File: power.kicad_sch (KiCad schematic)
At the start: 37 parts, among them J6 Conn_01x02, Q1 AO3401A, SW1 MSK12C02, U1 TP4056-42-ESOP8, U2 EA3036C

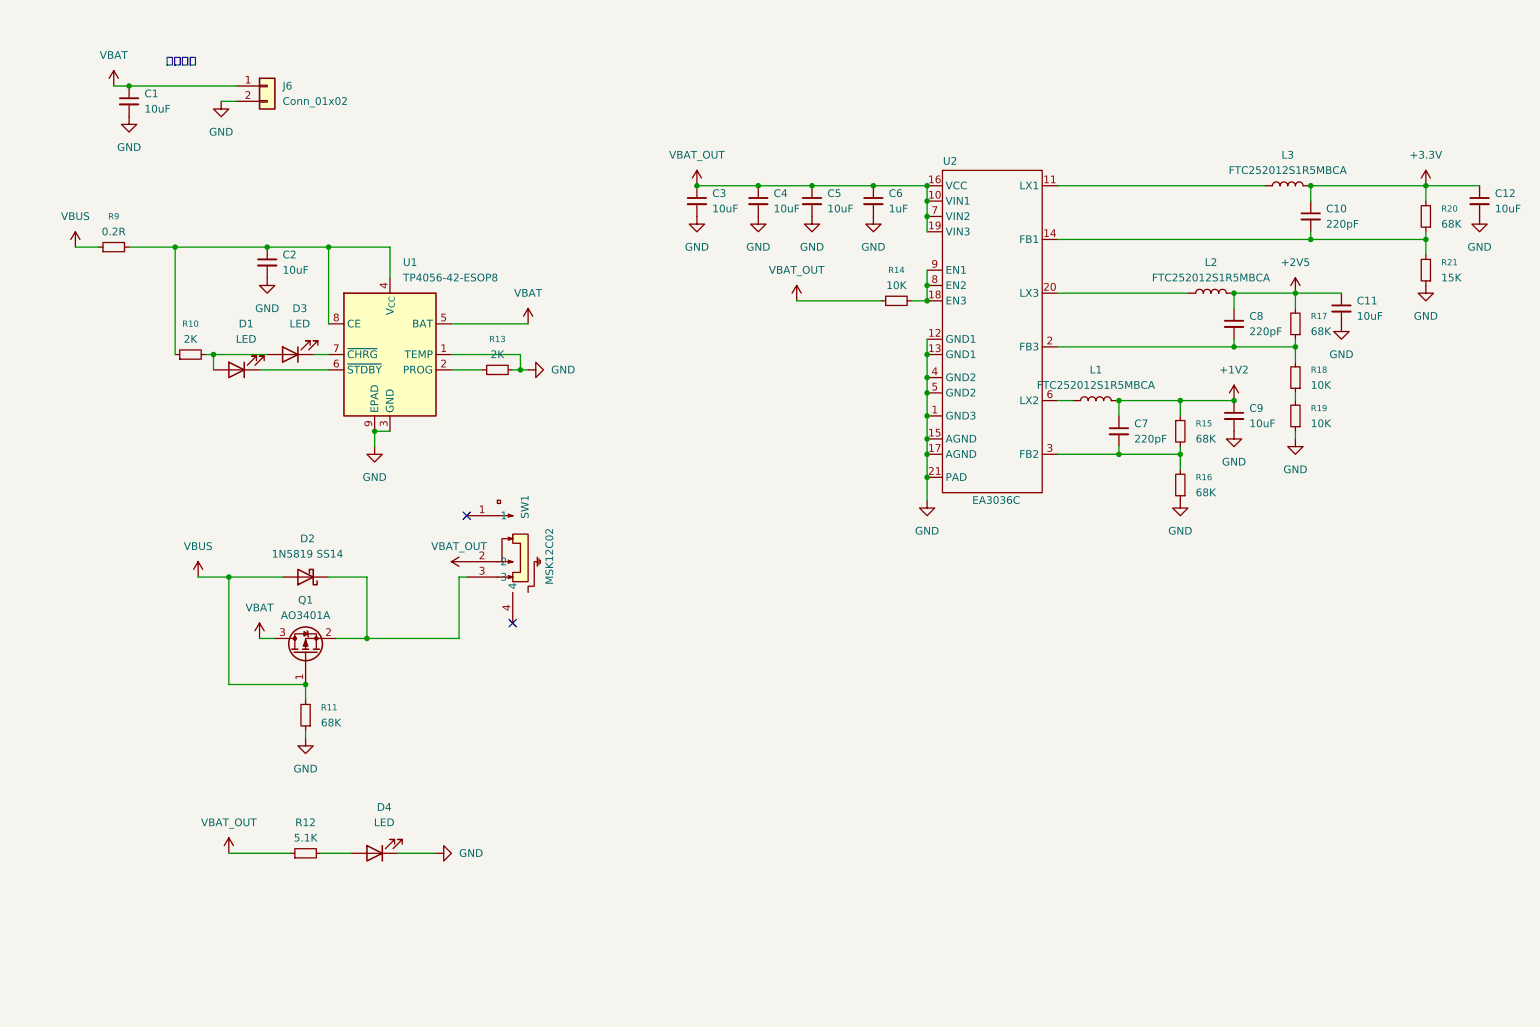
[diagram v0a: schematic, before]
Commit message: V0.3.1 bugfix
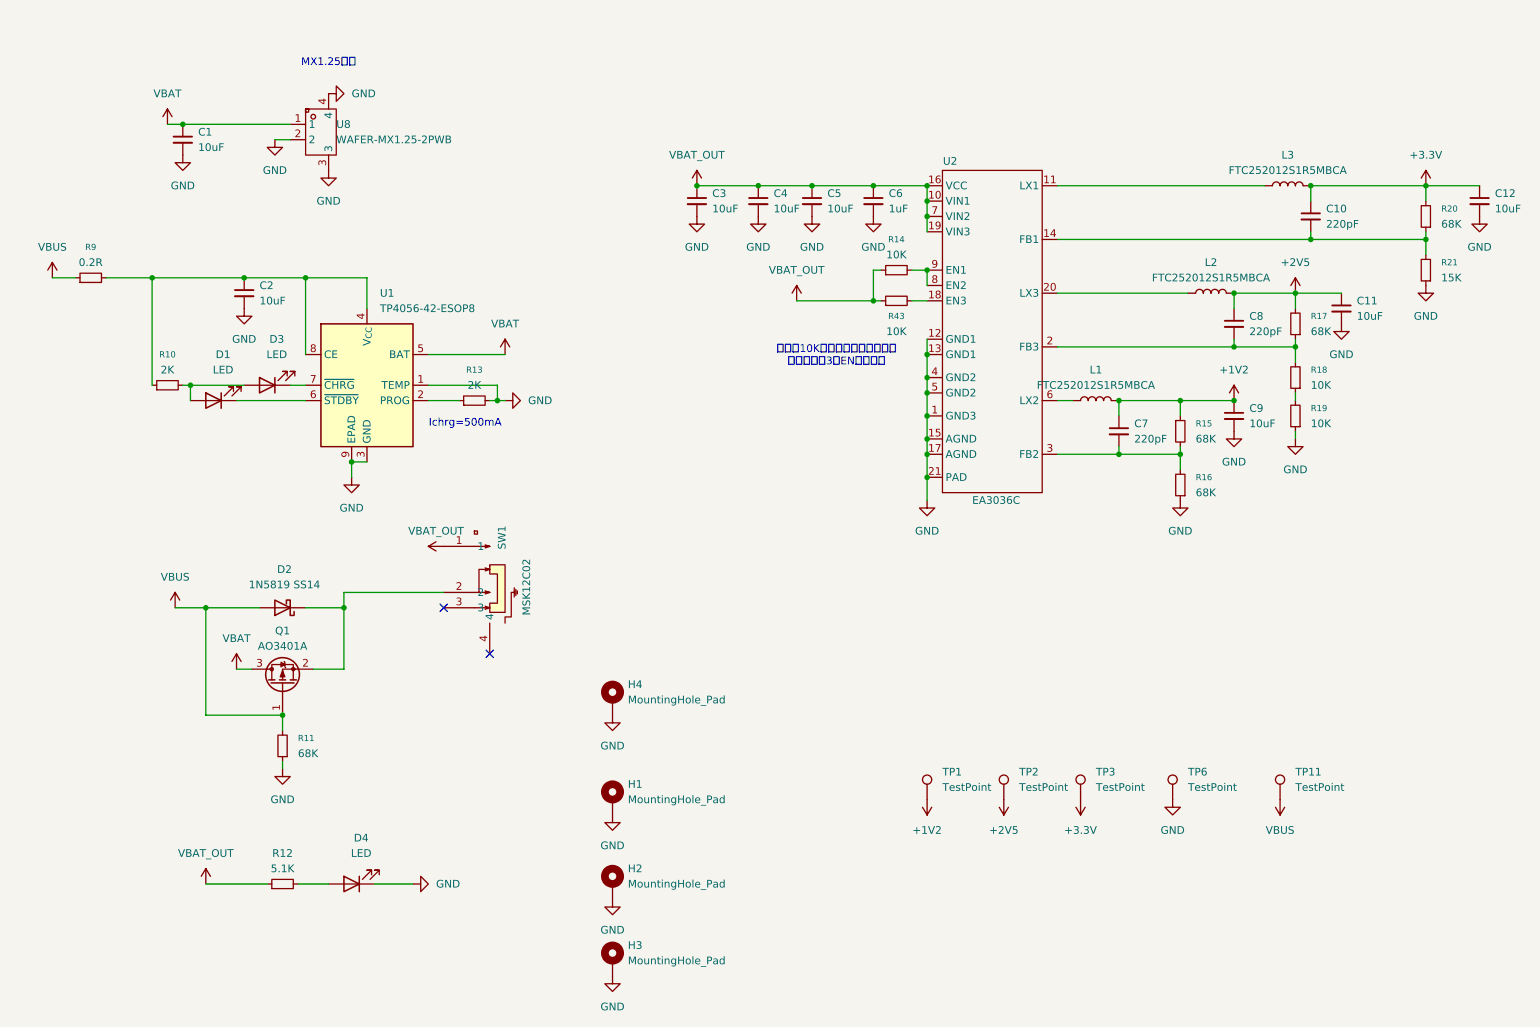
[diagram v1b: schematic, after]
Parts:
- removed J6: Conn_01x02, EasyEDA:CONN-SMD_2P-P1.25_XUNPU_WAFER-MX1.25-2PWB, symbol Connector_Generic:Conn_01x02
- added H1, H2, H3, H4: MountingHole_Pad, MountingHole:MountingHole_2.7mm_M2.5_DIN965_Pad, symbol Mechanical:MountingHole_Pad
- added R43: 10K, Resistor_SMD:R_0603_1608Metric, symbol Device:R_Small
- added TP1, TP11, TP2, TP3, TP6: TestPoint, TestPoint:TestPoint_Pad_D1.5mm, symbol Connector:TestPoint
- added U8: WAFER-MX1.25-2PWB, EasyEDA:CONN-SMD_2P-P1.25_XUNPU_WAFER-MX1.25-2PWB, symbol EasyEDA:WAFER-MX1.25-2PWB
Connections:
- net +1V2: now also TP1.1
- net +2V5: now also TP2.1
- net +3.3V: now also TP3.1
- net GND: now also H1.1, H2.1, H3.1, H4.1, TP6.1, U8.2, U8.3, U8.4
- net VBAT: now also U8.1
- net VBAT_OUT: now also SW1.1, R43.1; no longer SW1.2
- net VBUS: now also TP11.1
- net at R14.2, U2.8 (EN2), U2.9 (EN1): no longer U2.18 (EN3)
- net at D2.1 (K), Q1.2 (S): now also SW1.2; no longer SW1.3
- new net: R43.2, U2.18 (EN3)
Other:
- note added: "Ichrg=500mA"
- note added: "MX1.25端子"
- note added: "此处双10K电阻是为了走线方便。 和单电阻带3个EN效果一致"
- note removed: "正常电池"
- moved on the sheet: C1, C2, D1, D2, D3, D4, Q1, R10, R11, R12, R13, R14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

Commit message: V0.5
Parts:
- removed R43: 10K, Resistor_SMD:R_0603_1608Metric, symbol Device:R_Small
- removed SW1: MSK12C02, EasyEDA:SW-TH_MSK12C02, symbol EasyEDA:MSK12C02
- removed U8: WAFER-MX1.25-2PWB, EasyEDA:CONN-SMD_2P-P1.25_XUNPU_WAFER-MX1.25-2PWB, symbol EasyEDA:WAFER-MX1.25-2PWB
- added C47: 100nF, Capacitor_SMD:C_0603_1608Metric, symbol Device:C_Small
- added C48: 10uF, Capacitor_SMD:C_0603_1608Metric, symbol Device:C_Small
- added Q2: AO3401A, Package_TO_SOT_SMD:SOT-23, symbol Transistor_FET:AO3401A
- added R32: 10K, Resistor_SMD:R_0603_1608Metric, symbol Device:R_Small
- added SW1: TS24CA, EasyEDA:SW-SMD_TS24CA, symbol EasyEDA_old:TS24CA
- added TP12: TestPoint, TestPoint:TestPoint_Pad_D1.0mm, symbol Connector:TestPoint
- added U10: ZX-SH1.0-2PWT, EasyEDA:CONN-SMD_2P-P1.00_HX-1.0-2P-WT, symbol EasyEDA:ZX-SH1.0-2PWT
- added U8: GEK100-XX, Package_TO_SOT_SMD:SOT-23-6, symbol shirogane:GEK100-XX
- D2: value 1N5819 SS14 -> 1N5819WS
- R13: value 2K -> 5.1K
- TP1, TP11, TP2, TP3, TP6: footprint TestPoint:TestPoint_Pad_D1.5mm -> TestPoint:TestPoint_Pad_D1.0mm
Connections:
- net +3.3V: now also R12.1
- net GND: now also R14.1, C47.2, C48.2, SW1.1, SW1.2, SW1.3, U10.2, U10.3, U10.4, U8.2 (GND)
- net VBAT: now also C47.1, TP12.1, U10.1, U8.1 (VDD)
- net VBAT_OUT: now also C48.1, Q2.3 (D), R32.2; no longer R12.1, R14.1
- net at U2.18 (EN3): now also U2.8 (EN2), U2.9 (EN1), R32.1
- net at R13.1, U1.2 (PROG): now also R14.2
- net at D2.1 (K), Q1.2 (S): now also Q2.2 (S)
- new net: SW1.4, U8.3 (KEY)
- new net: Q2.1 (G), U8.5 (OUTL)
- new net PWR_SHUTDOWN: U8.4 (RST)
- no-connect marks 2 -> 1
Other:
- note added: "SH1.0端子"
- note added: "按键开关机（低压保护也靠这个切断） 感谢群友：“你说得对”、星语Studio、土豆、量子！"
- note added: "电池规格书要求充电电流：0.2C 300mA Rchrg=3.38k Ichrg=296mA"
- note removed: "Ichrg=500mA"
- note removed: "MX1.25端子"
- note removed: "此处双10K电阻是为了走线方便。 和单电阻带3个EN效果一致"
- moved on the sheet: C1, C2, D1, D2, D3, H1, H2, H3, H4, Q1, R10, R11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
